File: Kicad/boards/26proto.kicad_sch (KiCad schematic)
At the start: 36 parts, among them J1 5051104096, J2 Micro_SD_Card, J3 URM37, J4 RE12A, J5 RS485_TFT, J6 RS485_airdata, J7 RS485_logger_2, J8 RS485_logger, J9 BNO085, Q2 NPN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

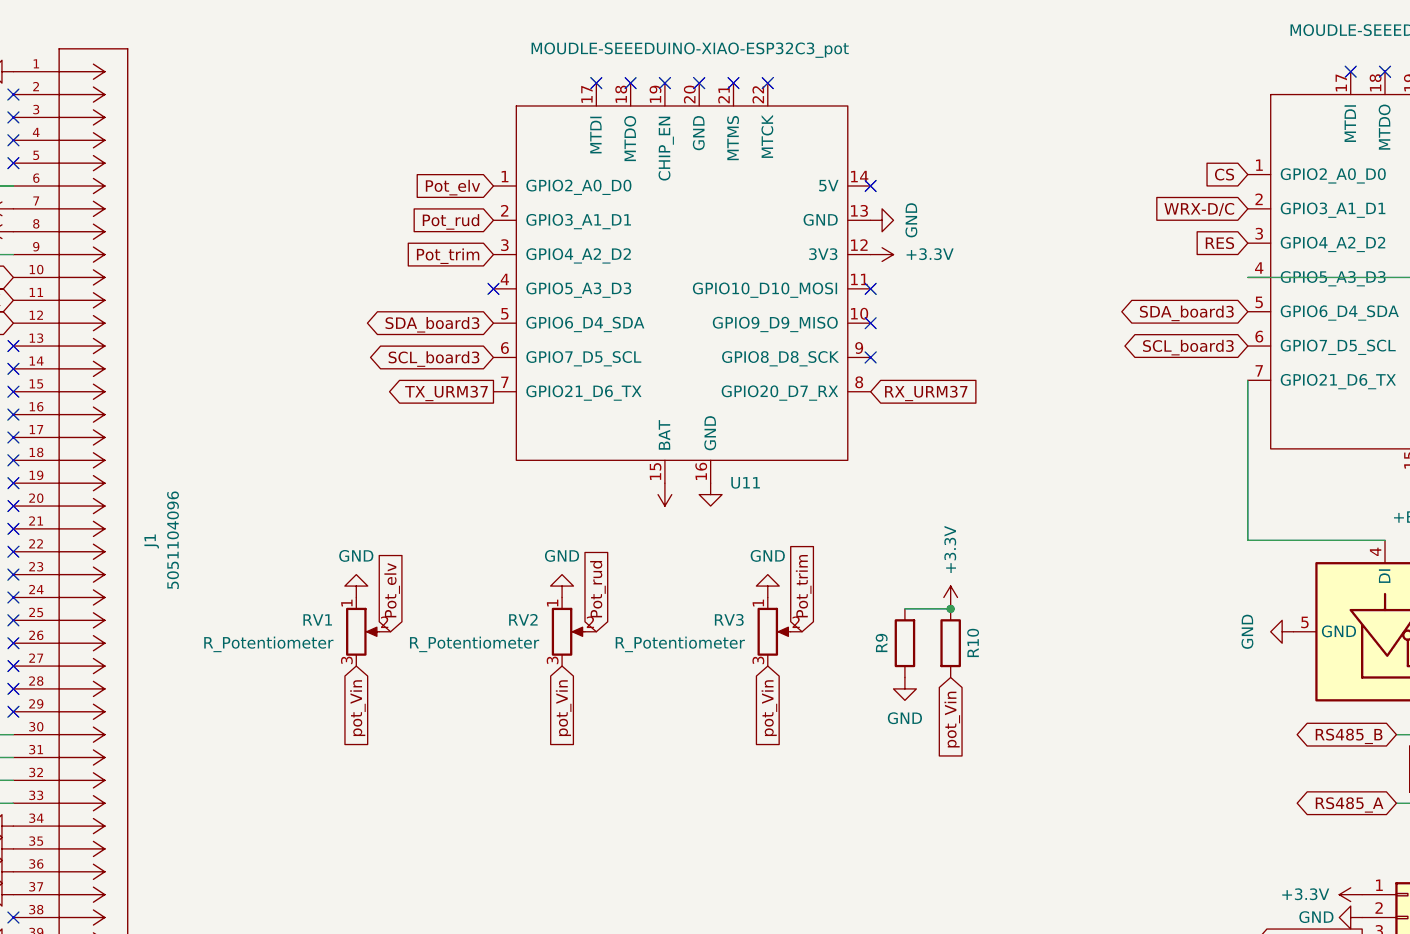
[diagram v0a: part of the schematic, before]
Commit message: updated TFT and sensors board
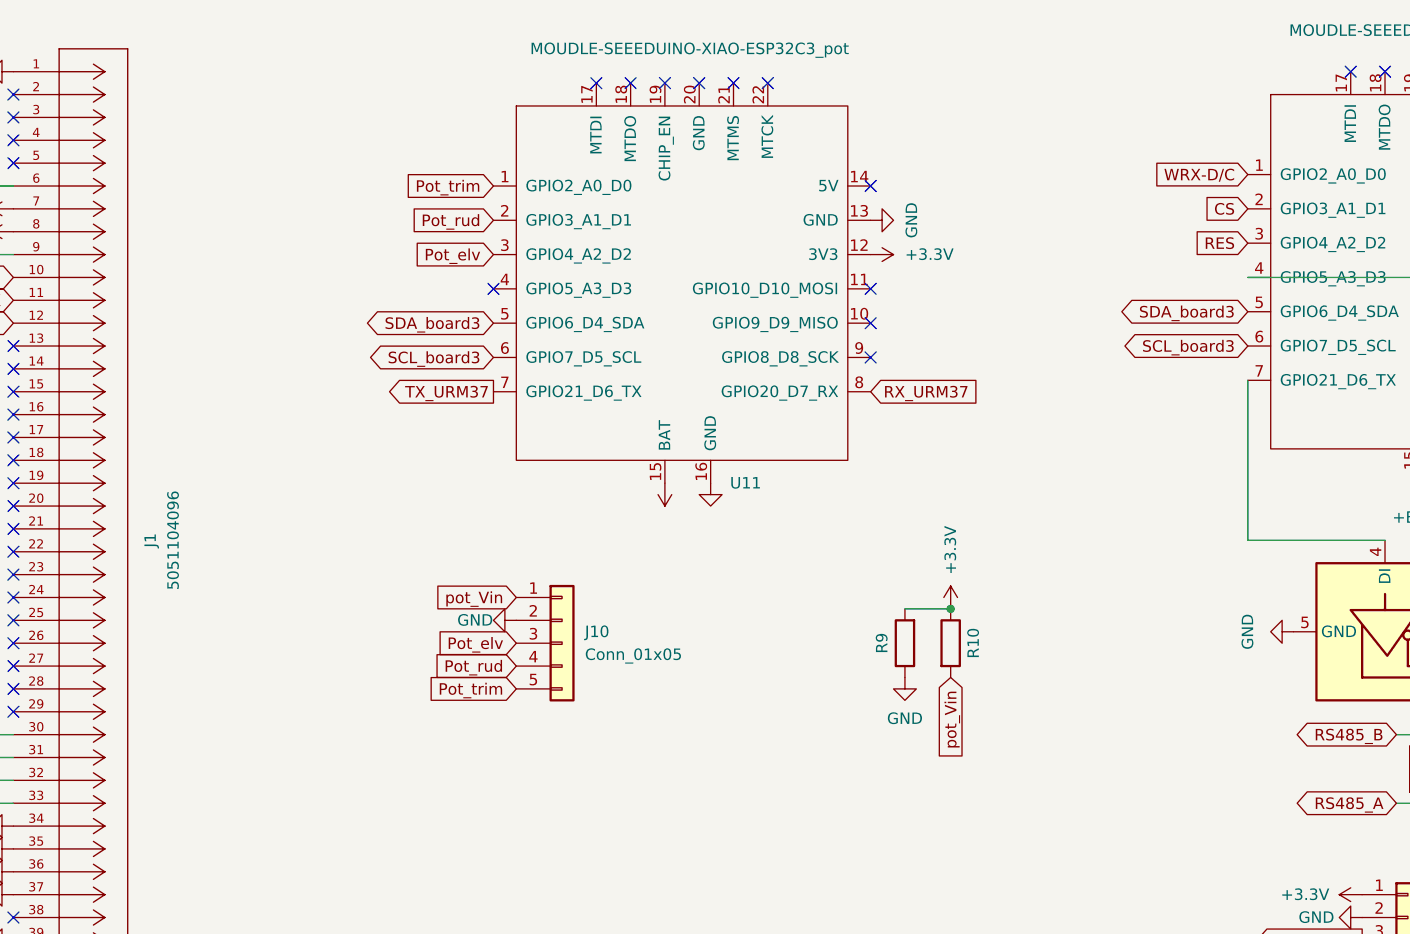
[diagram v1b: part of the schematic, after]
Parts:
- removed RV1, RV2, RV3: R_Potentiometer, Connector_JST:JST_XH_S3B-XH-SM4-TB_1x03-1MP_P2.50mm_Horizontal, symbol Device:R_Potentiometer
- added J10: Conn_01x05, Connector_JST:JST_PH_S5B-PH-SM4-TB_1x05-1MP_P2.00mm_Horizontal, symbol Connector_Generic:Conn_01x05
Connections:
- net CS: now also U1.2 (GPIO3_A1_D1); no longer U1.1 (GPIO2_A0_D0)
- net GND: now also J10.2 (Pin_2)
- net Pot_elv: now also U11.3 (GPIO4_A2_D2), J10.3 (Pin_3); no longer U11.1 (GPIO2_A0_D0)
- net Pot_rud: now also J10.4 (Pin_4)
- net Pot_trim: now also U11.1 (GPIO2_A0_D0), J10.5 (Pin_5); no longer U11.3 (GPIO4_A2_D2)
- net WRX-D/C: now also U1.1 (GPIO2_A0_D0); no longer U1.2 (GPIO3_A1_D1)
- net pot_Vin: now also J10.1 (Pin_1)

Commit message: updated logger and IMU board
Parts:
- added R11, R12, R13: R, Resistor_SMD:R_0201_0603Metric_Pad0.64x0.40mm_HandSolder, symbol Device:R
- J9: footprint footprints:MODULE_4754 -> 4754:MODULE_4754; symbol Connector_Generic:Conn_01x04 -> 4754:4754; MANUFACTURER (none) -> Adafruit; MAXIMUM_PACKAGE_HEIGHT (none) -> 4.6mm; PARTREV (none) -> 2021-03-16; SNAPEDA_PN (none) -> 4754; STANDARD (none) -> Manufacturer Recommendations
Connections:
- net +3.3V: now also J9.JP1_1 (VIN), R11.2, R12.1, R13.2; no longer J9.1 (Pin_1)
- net CS_SD: now also U5.4 (GPIO5_A3_D3); no longer U5.1 (GPIO2_A0_D0)
- net GND: now also J9.JP1_3 (GND); no longer J9.2 (Pin_2)
- net Pot_elv: now also U11.1 (GPIO2_A0_D0); no longer U11.3 (GPIO4_A2_D2)
- net Pot_trim: now also U11.3 (GPIO4_A2_D2); no longer U11.1 (GPIO2_A0_D0)
- net RX_URM37: now also J3.4 (Pin_4); no longer J3.3 (Pin_3)
- net SCLK_SD: now also R13.1
- net SCL_BNO085: now also J9.JP1_4 (SCL); no longer J9.4 (Pin_4)
- net SCL_board3: now also R12.2
- net SDA_BNO085: now also J9.JP1_5 (SDA); no longer J9.3 (Pin_3)
- net SDA_board3: now also R11.1
- net TX_URM37: now also J3.3 (Pin_3); no longer J3.4 (Pin_4)
- net at U2.2 (~{RE}), U2.3 (DE): now also U5.1 (GPIO2_A0_D0); no longer U5.4 (GPIO5_A3_D3)
- no-connect marks 73 -> 82

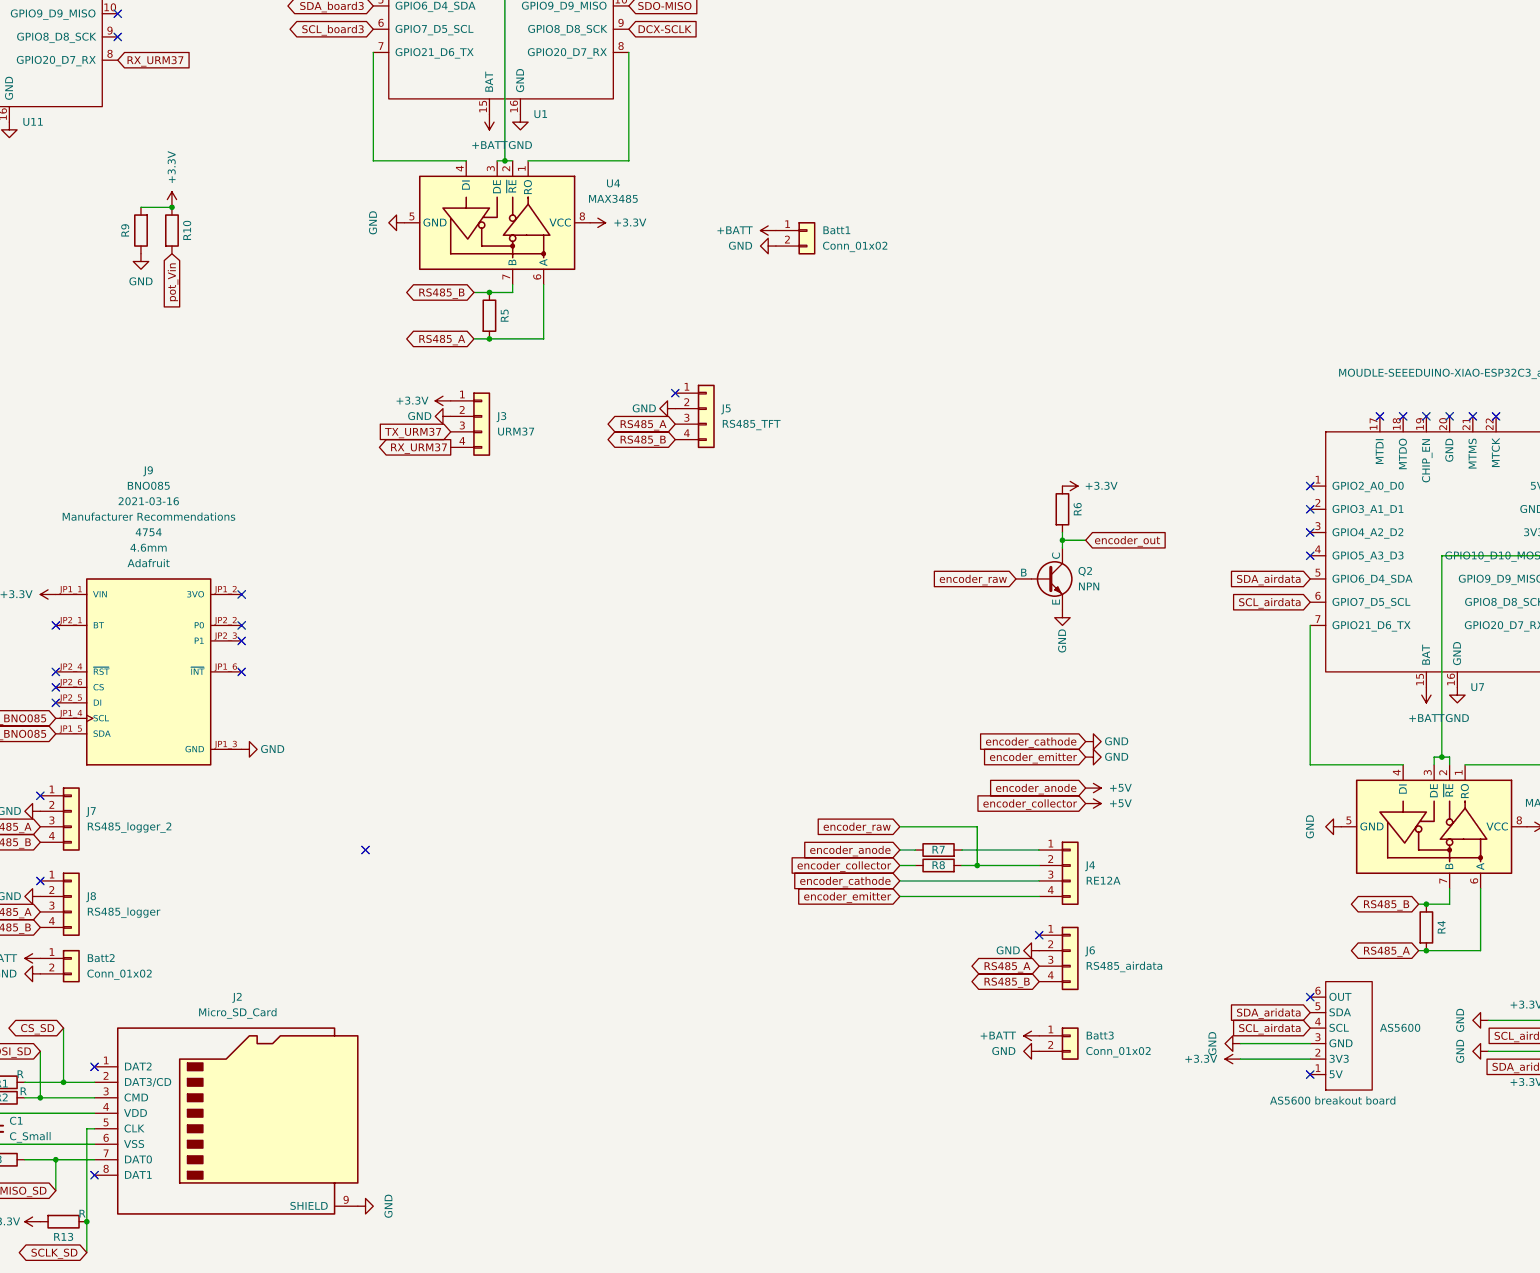
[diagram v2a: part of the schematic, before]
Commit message: updated IMU board
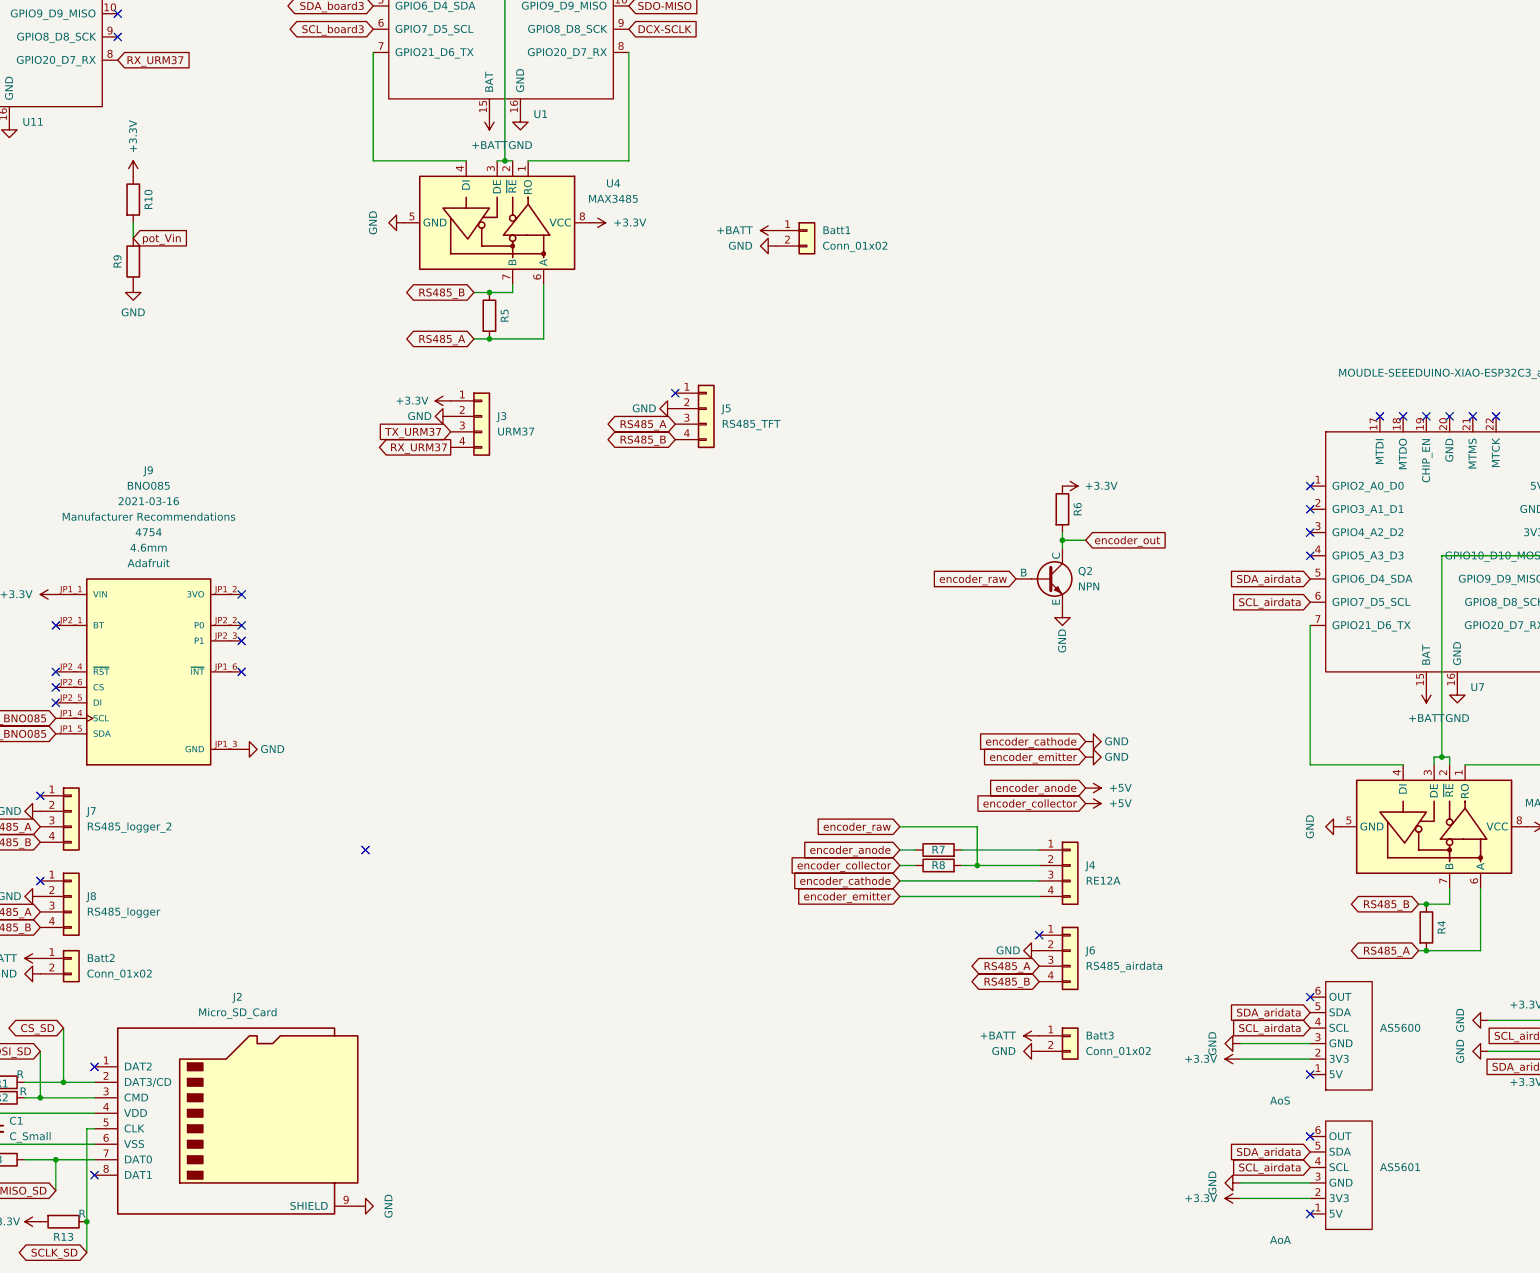
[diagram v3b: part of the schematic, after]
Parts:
- added AS5601: AoA, Connector_PinHeader_2.54mm:PinHeader_1x06_P2.54mm_Vertical, symbol New_Library:AS5600
- AS5600: value AS5600 breakout board -> AoS
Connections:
- net +3.3V: now also AS5601.2 (3V3); no longer R9.2
- net GND: now also AS5601.3 (GND)
- net SCL_airdata: now also AS5601.4 (SCL)
- net SDA_aridata: now also AS5601.5 (SDA)
- net pot_Vin: now also R9.2
- no-connect marks 82 -> 84
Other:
- moved on the sheet: R10, R9

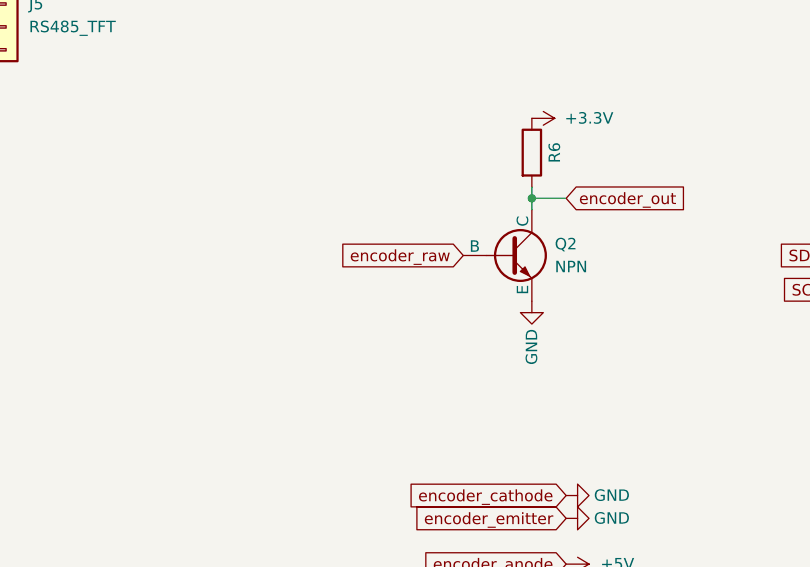
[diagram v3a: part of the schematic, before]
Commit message: edited airdata board
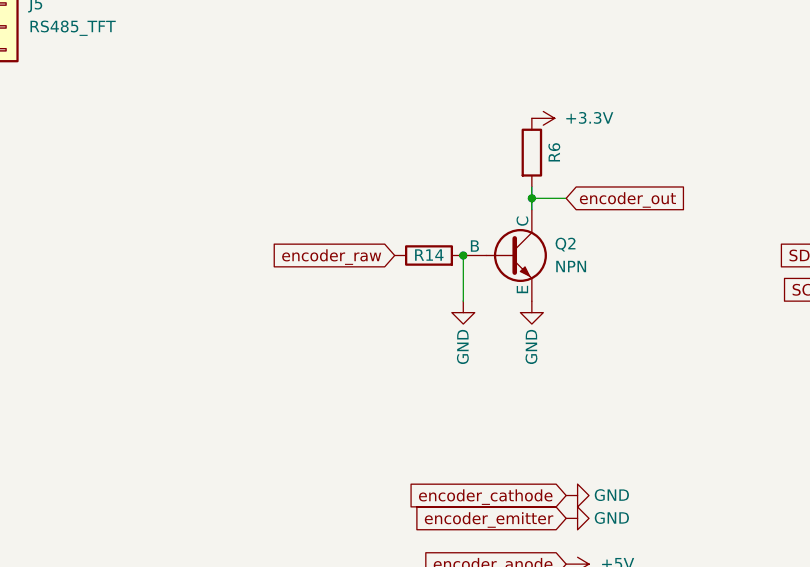
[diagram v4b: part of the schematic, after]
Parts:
- added R14: R, Resistor_SMD:R_0201_0603Metric_Pad0.64x0.40mm_HandSolder, symbol Device:R
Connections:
- net GND: now also Q2.2 (B), R14.2
- net encoder_raw: now also R14.1; no longer Q2.2 (B)
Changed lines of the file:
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@@
 	)
 	(junction
+		(at 288.29 146.05)
+		(diameter 0)
+		(color 0 0 0 0)
+	)
+	(junction
 		(at 358.14 175.26)
 		(diameter 0)
@@
 	(wire
 		(pts
+			(xy 288.29 146.05) (xy 288.29 151.13)
+		)
+		(stroke
+			(width 0)
+			(type default)
+		)
+	)
+	(wire
+		(pts
 			(xy 76.2 233.68) (xy 77.47 233.68)
 		)
@@
 	(wire
 		(pts
-			(xy 361.95 176.53) (xy 378.46 176.53)
+			(xy 299.72 139.7) (xy 295.91 139.7)
 		)
 		(stroke
@@
 	(wire
 		(pts
-			(xy 279.4 193.04) (xy 281.94 193.04)
+			(xy 361.95 176.53) (xy 378.46 176.53)
 		)
 		(stroke
@@
 	(wire
 		(pts
-			(xy 295.91 139.7) (xy 295.91 140.97)
+			(xy 279.4 193.04) (xy 281.94 193.04)
 		)
 		(stroke
@@
 	(wire
 		(pts
-			(xy 41.91 106.68) (xy 45.72 106.68)
+			(xy 295.91 139.7) (xy 295.91 140.97)
 		)
 		(stroke
@@
 	(wire
 		(pts
-			(xy 199.39 99.06) (xy 201.93 99.06)
+			(xy 41.91 106.68) (xy 45.72 106.68)
 		)
 		(stroke
@@
 	(wire
 		(pts
-			(xy 279.4 190.5) (xy 292.1 190.5)
+			(xy 199.39 99.06) (xy 201.93 99.06)
 		)
 		(stroke
@@
 	(wire
 		(pts
-			(xy 295.91 139.7) (xy 299.72 139.7)
+			(xy 279.4 190.5) (xy 292.1 190.5)
 		)
 		(stroke
@@
 	(global_label "encoder_raw"
 		(shape input)
-		(at 288.29 146.05 180)
+		(at 280.67 146.05 180)
 		(fields_autoplaced yes)
 		(effects
@@
 		)
 		(property "Intersheetrefs" "${INTERSHEET_REFS}"
-			(at 273.5725 146.05 0)
+			(at 265.9525 146.05 0)
 			(effects
 				(font
@@
 	)
 	(symbol
+		(lib_id "Device:R")
+		(at 284.48 146.05 90)
+		(unit 1)
+		(exclude_from_sim no)
+		(in_bom yes)
+		(on_board yes)
+		(dnp no)
+		(property "Reference" "R14"
+			(at 284.48 146.05 90)
+			(effects
+				(font
+					(size 1.27 1.27)
+				)
+			)
+		)
+		(property "Value" "R"
+			(at 281.432 147.32 90)
+			(effects
+				(font
+					(size 1.27 1.27)
+				)
+				(hide yes)
+			)
+		)
+		(property "Footprint" "Resistor_SMD:R_0201_0603Metric_Pad0.64x0.40mm_HandSolder"
+			(at 284.48 147.828 90)
+			(effects
+				(font
+					(size 1.27 1.27)
+				)
+				(hide yes)
+			)
+		)
+		(property "Datasheet" "~"
+			(at 284.48 146.05 0)
+			(effects
+				(font
+					(size 1.27 1.27)
+				)
+				(hide yes)
+			)
+		)
+		(property "Description" "Resistor"
+			(at 284.48 146.05 0)
+			(effects
+				(font
+					(size 1.27 1.27)
+				)
+				(hide yes)
+			)
+		)
+		(pin "1"
+		)
+		(pin "2"
+		)
+		(instances
+			(project "26proto"
+				(path "/493bec57-bd9f-4f18-b3ef-0d7a091ad475"
+					(reference "R14")
+					(unit 1)
+				)
+			)
+		)
+	)
+	(symbol
 		(lib_id "power:+3.3V")
 		(at 118.11 241.3 90)
@@
 					(unit 1)
 				)
+			)
+		)
+	)
+	(symbol
+		(lib_id "power:GND")
+		(at 288.29 151.13 0)
+		(unit 1)
+		(exclude_from_sim no)
+		(in_bom yes)
+		(on_board yes)
+		(dnp no)
+		(property "Reference" "#PWR057"
+			(at 288.29 157.48 0)
+			(effects
+				(font
+					(size 1.27 1.27)
+				)
+				(hide yes)
+			)
+		)
+		(property "Value" "GND"
+			(at 288.29 156.21 90)
+			(effects
+				(font
+					(size 1.27 1.27)
+				)
+			)
+		)
+		(property "Footprint" ""
+			(at 288.29 151.13 0)
+			(effects
+				(font
+					(size 1.27 1.27)
+				)
+				(hide yes)
+			)
+		)
+		(property "Datasheet" ""
+			(at 288.29 151.13 0)
+			(effects
+				(font
+					(size 1.27 1.27)
+				)
+				(hide yes)
+			)
+		)
+		(property "Description" "Power symbol creates a global label with name \"GND\" , ground"
+			(at 288.29 151.13 0)
+			(effects
+				(font
+					(size 1.27 1.27)
+				)
+				(hide yes)
+			)
+		)
+		(pin "1"
+		)
+		(instances
+			(project "26proto"
+				(path "/493bec57-bd9f-4f18-b3ef-0d7a091ad475"
+					(reference "#PWR057")
+					(unit 1)
+				)
